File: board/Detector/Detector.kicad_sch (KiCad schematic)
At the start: 6 parts, among them J3 Conn_01x03, U3 LP2950-3.3_TO92

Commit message: Complete layout with top pour
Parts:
- C11, C12: footprint Capacitor_SMD:C_0805_2012Metric_Pad1.18x1.45mm_HandSolder -> Capacitor_SMD:C_1206_3216Metric_Pad1.33x1.80mm_HandSolder
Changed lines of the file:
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@@
       (effects (font (size 1.27 1.27)) (justify left))
     )
-    (property "Footprint" "Capacitor_SMD:C_0805_2012Metric_Pad1.18x1.45mm_HandSolder" (id 2) (at 187.6552 90.17 0)
+    (property "Footprint" "Capacitor_SMD:C_1206_3216Metric_Pad1.33x1.80mm_HandSolder" (id 2) (at 187.6552 90.17 0)
       (effects (font (size 1.27 1.27)) hide)
     )
@@
       (effects (font (size 1.27 1.27)) (justify left))
     )
-    (property "Footprint" "Capacitor_SMD:C_0805_2012Metric_Pad1.18x1.45mm_HandSolder" (id 2) (at 216.8652 90.17 0)
+    (property "Footprint" "Capacitor_SMD:C_1206_3216Metric_Pad1.33x1.80mm_HandSolder" (id 2) (at 216.8652 90.17 0)
       (effects (font (size 1.27 1.27)) hide)
     )
@@
     )
     (path "/85d90695-c34a-4d53-a278-d84dc76420c9"
-      (reference "C11") (unit 1) (value "10uf") (footprint "Capacitor_SMD:C_0805_2012Metric_Pad1.18x1.45mm_HandSolder")
+      (reference "C11") (unit 1) (value "10uf") (footprint "Capacitor_SMD:C_1206_3216Metric_Pad1.33x1.80mm_HandSolder")
     )
     (path "/7cb41dd2-1aab-4ecf-8548-867fc9c2354e"
-      (reference "C12") (unit 1) (value "10uf") (footprint "Capacitor_SMD:C_0805_2012Metric_Pad1.18x1.45mm_HandSolder")
+      (reference "C12") (unit 1) (value "10uf") (footprint "Capacitor_SMD:C_1206_3216Metric_Pad1.33x1.80mm_HandSolder")
     )
     (path "/3163ae8c-05cc-42f1-a236-f506d507cea3/031183ec-7451-4b6d-a9c0-62c89cc4ef82"

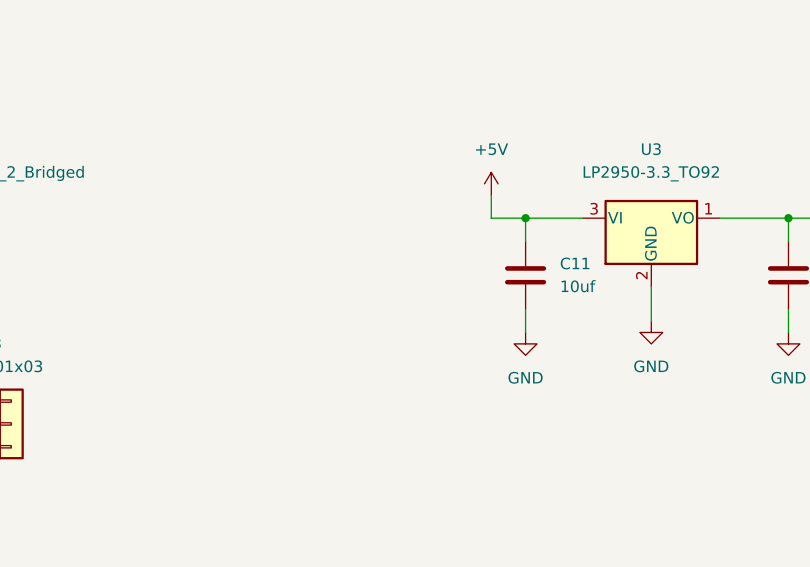
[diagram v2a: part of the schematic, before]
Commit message: Detector changes to better control overall bias level
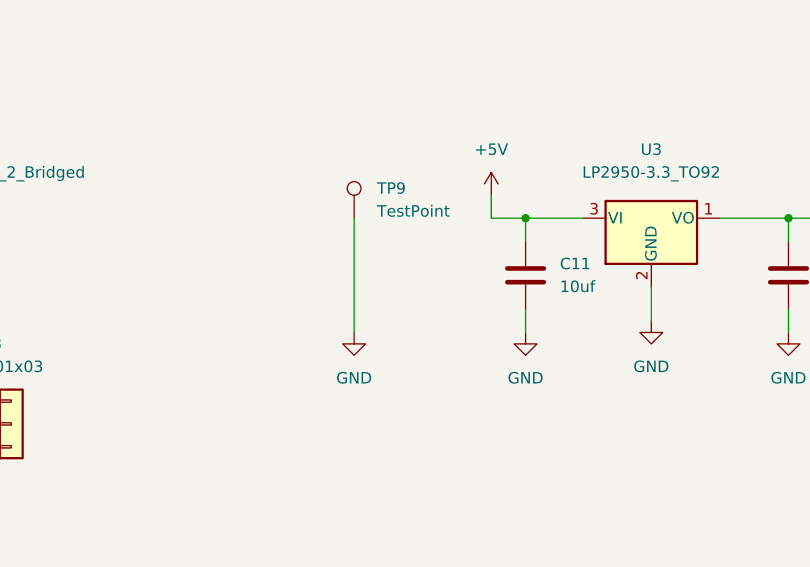
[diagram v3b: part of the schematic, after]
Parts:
- added TP9: TestPoint, Connector_PinHeader_2.54mm:PinHeader_1x01_P2.54mm_Vertical, symbol Connector:TestPoint
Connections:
- net GND: now also TP9.1

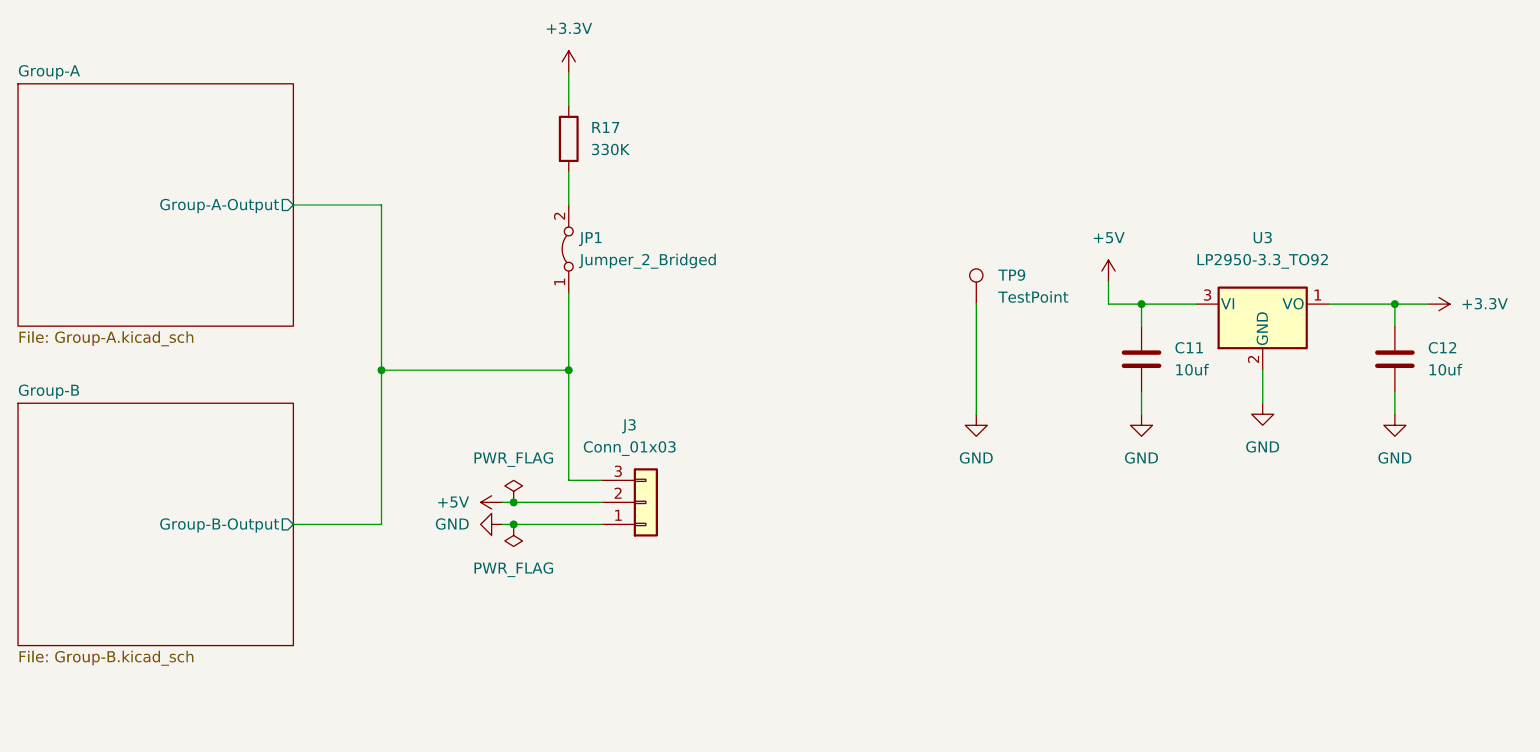
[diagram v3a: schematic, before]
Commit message: Changed connectors, 3D models, added test points
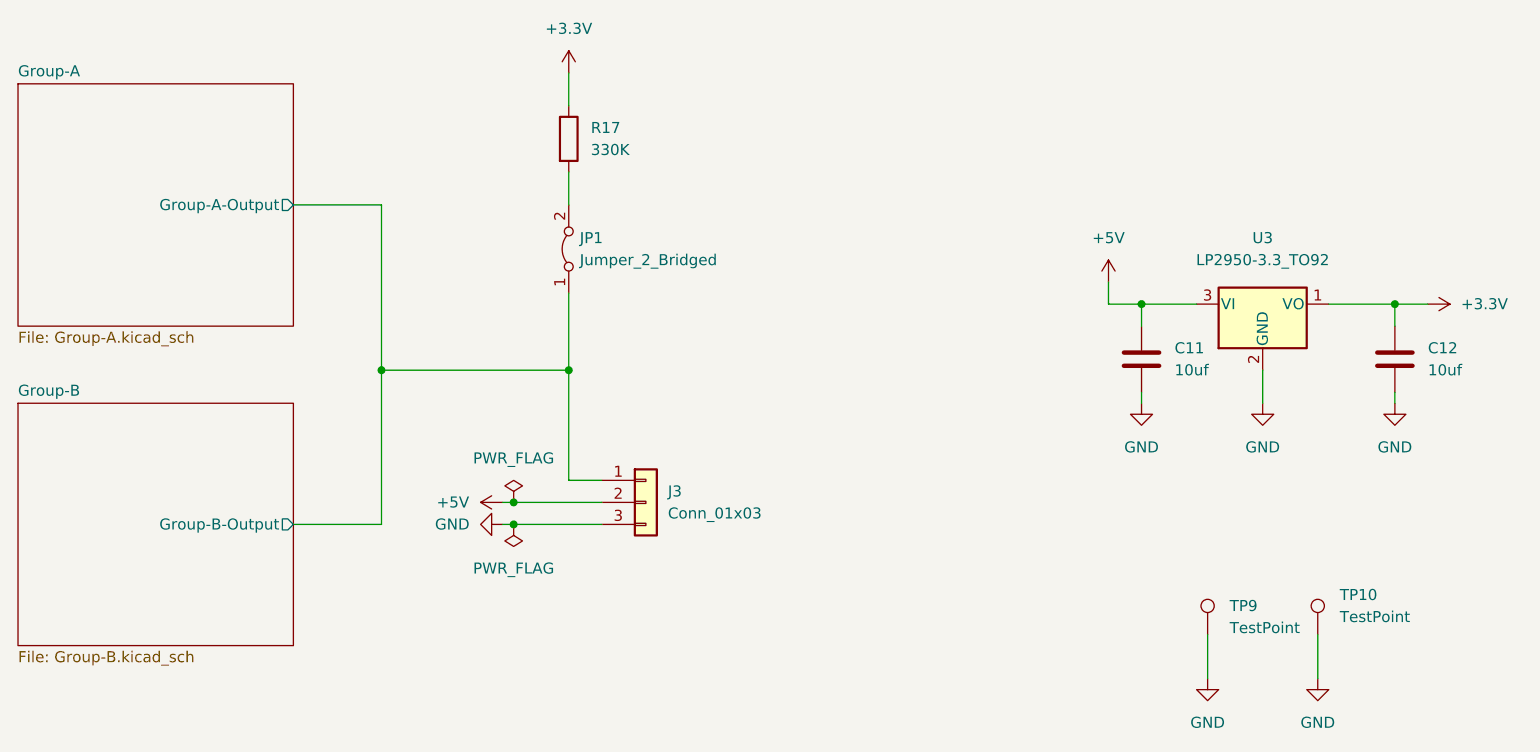
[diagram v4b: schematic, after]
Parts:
- added TP10: TestPoint, Connector_PinHeader_2.54mm:PinHeader_1x01_P2.54mm_Vertical, symbol Connector:TestPoint
- J3: footprint SaintGimp:KF2510_Header_1x03_Vertical -> TerminalBlock_TE-Connectivity:TerminalBlock_TE_282834-3_1x03_P2.54mm_Horizontal
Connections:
- net GND: now also J3.3 (Pin_3), TP10.1; no longer J3.1 (Pin_1)
- net Group-A/Group-A-Output: now also J3.1 (Pin_1); no longer J3.3 (Pin_3)
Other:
- moved on the sheet: TP9
